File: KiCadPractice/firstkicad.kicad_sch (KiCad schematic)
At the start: 12 parts, among them Q1 BC337, U1 LM358, U2 LM358

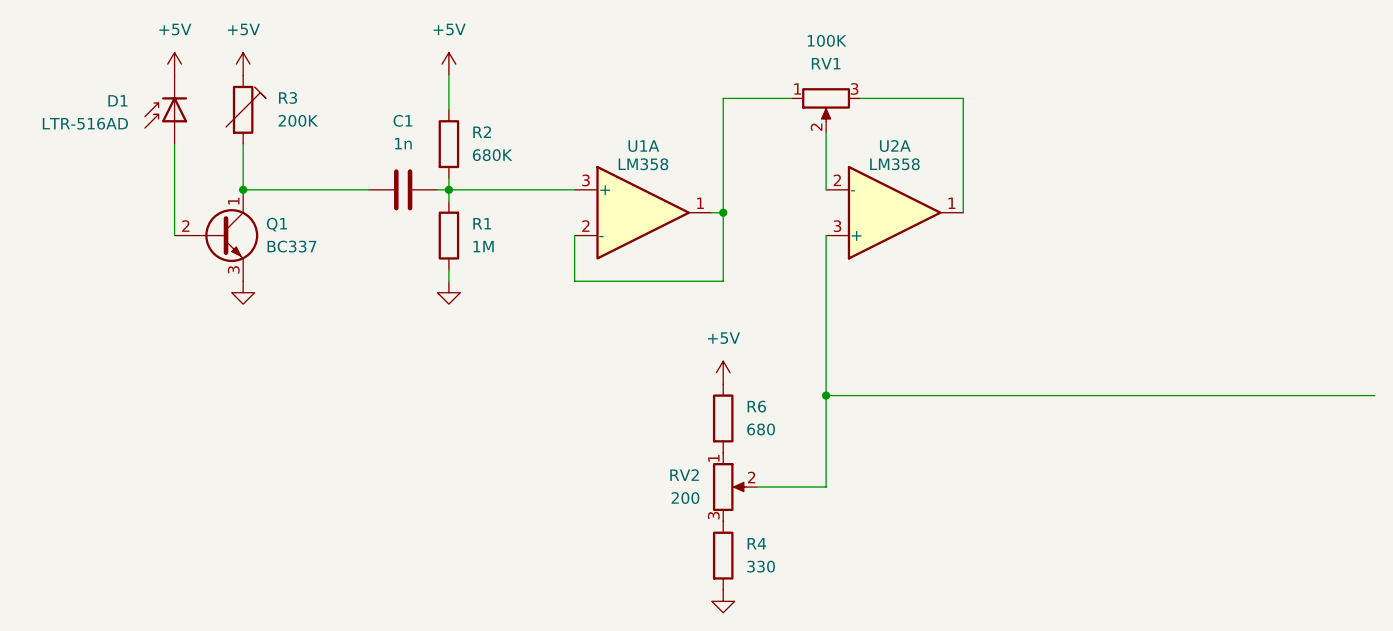
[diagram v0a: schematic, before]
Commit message: Fixed ERC issues.
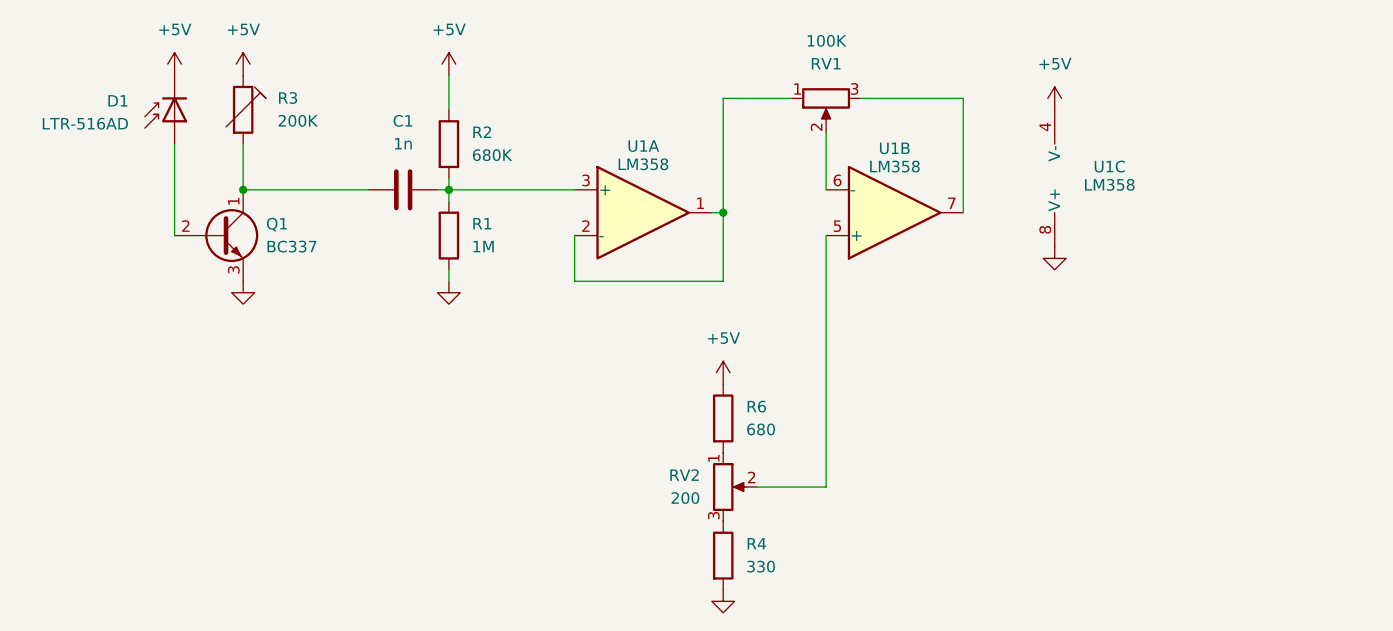
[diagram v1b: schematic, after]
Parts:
- added unit 3 of U1
- renumbered U2 to U1
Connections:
- net +5V: now also U1.4 (V-)
- net GND: now also U1.8 (V+)
- net at RV1.2: now also U1.6 (-); no longer U1.2 (-)
- net at RV1.3: now also U1.7; no longer U1.1
- net at RV2.2: now also U1.5 (+); no longer U1.3 (+)
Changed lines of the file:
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@@
 		(color 0 0 0 0)
 	)
-	(junction
-		(at 148.59 77.47)
-		(diameter 0)
-		(color 0 0 0 0)
-	)
 	(wire
 		(pts
@@
 	(wire
 		(pts
-			(xy 148.59 87.63) (xy 148.59 77.47)
+			(xy 148.59 59.69) (xy 148.59 87.63)
 		)
 		(stroke
@@
 	(wire
 		(pts
-			(xy 148.59 77.47) (xy 209.55 77.47)
-		)
-		(stroke
-			(width 0)
-			(type default)
-		)
-	)
-	(wire
-		(pts
 			(xy 106.68 54.61) (xy 120.65 54.61)
 		)
@@
 		(pts
 			(xy 83.82 54.61) (xy 97.79 54.61)
-		)
-		(stroke
-			(width 0)
-			(type default)
-		)
-	)
-	(wire
-		(pts
-			(xy 148.59 77.47) (xy 148.59 59.69)
 		)
 		(stroke
@@
 	(symbol
 		(lib_id "power:GND")
+		(at 173.99 60.96 0)
+		(unit 1)
+		(exclude_from_sim no)
+		(in_bom yes)
+		(on_board yes)
+		(dnp no)
+		(fields_autoplaced yes)
+		(property "Reference" "#PWR09"
+			(at 173.99 67.31 0)
+			(effects
+				(font
+					(size 1.27 1.27)
+				)
+				(hide yes)
+			)
+		)
+		(property "Value" "GND"
+			(at 173.99 66.04 0)
+			(effects
+				(font
+					(size 1.27 1.27)
+				)
+				(hide yes)
+			)
+		)
+		(property "Footprint" ""
+			(at 173.99 60.96 0)
+			(effects
+				(font
+					(size 1.27 1.27)
+				)
+				(hide yes)
+			)
+		)
+		(property "Datasheet" ""
+			(at 173.99 60.96 0)
+			(effects
+				(font
+					(size 1.27 1.27)
+				)
+				(hide yes)
+			)
+		)
+		(property "Description" "Power symbol creates a global label with name \"GND\" , ground"
+			(at 173.99 60.96 0)
+			(effects
+				(font
+					(size 1.27 1.27)
+				)
+				(hide yes)
+			)
+		)
+		(pin "1"
+		)
+		(instances
+			(project "firstkicad"
+				(path "/6a1506e1-f232-4ea9-a704-c10ff0d0d683"
+					(reference "#PWR09")
+					(unit 1)
+				)
+			)
+		)
+	)
+	(symbol
+		(lib_id "power:GND")
 		(at 137.16 99.06 0)
 		(unit 1)
@@
 	)
 	(symbol
+		(lib_id "Amplifier_Operational:LM358")
+		(at 176.53 53.34 0)
+		(mirror x)
+		(unit 3)
+		(exclude_from_sim no)
+		(in_bom yes)
+		(on_board yes)
+		(dnp no)
+		(property "Reference" "U1"
+			(at 180.086 52.07 0)
+			(effects
+				(font
+					(size 1.27 1.27)
+				)
+			)
+		)
+		(property "Value" "LM358"
+			(at 180.086 54.102 0)
+			(effects
+				(font
+					(size 1.27 1.27)
+				)
+			)
+		)
+		(property "Footprint" "OptoDevice:Broadcom_APDS-9160-003"
+			(at 176.53 53.34 0)
+			(effects
+				(font
+					(size 1.27 1.27)
+				)
+				(hide yes)
+			)
+		)
+		(property "Datasheet" "http://www.ti.com/lit/ds/symlink/lm2904-n.pdf"
+			(at 176.53 53.34 0)
+			(effects
+				(font
+					(size 1.27 1.27)
+				)
+				(hide yes)
+			)
+		)
+		(property "Description" "Low-Power, Dual Operational Amplifiers, DIP-8/SOIC-8/TO-99-8"
+			(at 176.53 53.34 0)
+			(effects
+				(font
+					(size 1.27 1.27)
+				)
+				(hide yes)
+			)
+		)
+		(pin "8"
+		)
+		(pin "5"
+		)
+		(pin "6"
+		)
+		(pin "7"
+		)
+		(pin "2"
+		)
+		(pin "3"
+		)
+		(pin "1"
+		)
+		(pin "4"
+		)
+		(instances
+			(project "firstkicad"
+				(path "/6a1506e1-f232-4ea9-a704-c10ff0d0d683"
+					(reference "U1")
+					(unit 3)
+				)
+			)
+		)
+	)
+	(symbol
 		(lib_id "power:+5V")
 		(at 83.82 41.91 0)
@@
 		(at 156.21 57.15 0)
 		(mirror x)
-		(unit 1)
-		(exclude_from_sim no)
-		(in_bom yes)
-		(on_board yes)
-		(dnp no)
-		(property "Reference" "U2"
-			(at 156.21 49.784 0)
+		(unit 2)
+		(exclude_from_sim no)
+		(in_bom yes)
+		(on_board yes)
+		(dnp no)
+		(property "Reference" "U1"
+			(at 156.21 50.038 0)
 			(effects
 				(font
@@
 		)
 		(property "Value" "LM358"
-			(at 156.21 51.816 0)
+			(at 156.21 52.07 0)
 			(effects
 				(font
@@
 			(project ""
 				(path "/6a1506e1-f232-4ea9-a704-c10ff0d0d683"
-					(reference "U2")
-					(unit 1)
-				)
+					(reference "U1")
+					(unit 2)
+				)
+			)
+		)
+	)
+	(symbol
+		(lib_id "power:+5V")
+		(at 173.99 45.72 0)
+		(unit 1)
+		(exclude_from_sim no)
+		(in_bom yes)
+		(on_board yes)
+		(dnp no)
+		(fields_autoplaced yes)
+		(property "Reference" "#PWR07"
+			(at 173.99 49.53 0)
+			(effects
+				(font
+					(size 1.27 1.27)
+				)
+				(hide yes)
+			)
+		)
+		(property "Value" "+5V"
+			(at 173.99 40.64 0)
+			(effects
+				(font
+					(size 1.27 1.27)
+				)
+			)
+		)
+		(property "Footprint" ""
+			(at 173.99 45.72 0)
+			(effects
+				(font
+					(size 1.27 1.27)
+				)
+				(hide yes)
+			)
+		)
+		(property "Datasheet" ""
+			(at 173.99 45.72 0)
+			(effects
+				(font
+					(size 1.27 1.27)
+				)
+				(hide yes)
+			)
+		)
+		(property "Description" "Power symbol creates a global label with name \"+5V\""
+			(at 173.99 45.72 0)
+			(effects
+				(font
+					(size 1.27 1.27)
+				)
+				(hide yes)
+			)
+		)
+		(pin "1"
+		)
+		(instances
+			(project "firstkicad"
+				(path "/6a1506e1-f232-4ea9-a704-c10ff0d0d683"
+					(reference "#PWR07")
+					(unit 1)
+				)

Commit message: Fixed footprints.
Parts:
- C1: footprint Capacitor_THT:CP_Axial_L30.0mm_D18.0mm_P35.00mm_Horizontal -> Capacitor_SMD:C_1206_3216Metric_Pad1.33x1.80mm_HandSolder
- D1: footprint Diode_THT:D_A-405_P5.08mm_Vertical_KathodeUp -> Library:LTR-516AD
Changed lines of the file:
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@@
 			)
 		)
-		(property "Footprint" "Diode_THT:D_A-405_P5.08mm_Vertical_KathodeUp"
+		(property "Footprint" "Library:LTR-516AD"
 			(at 76.2 45.72 0)
 			(effects
@@
 			)
 		)
-		(property "Footprint" "Capacitor_THT:CP_Axial_L30.0mm_D18.0mm_P35.00mm_Horizontal"
+		(property "Footprint" "Capacitor_SMD:C_1206_3216Metric_Pad1.33x1.80mm_HandSolder"
 			(at 105.41 53.6448 0)
 			(effects

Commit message: Patched some more footprints.
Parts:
- Q1: footprint Transformer_THT:Autotransformer_Toroid_1Tap_Horizontal_D10.5mm_Amidon-T37 -> Package_TO_SOT_THT:TO-92L_Inline
- R1, R2, R3, R4, R6: footprint Resistor_THT:R_Axial_DIN0204_L3.6mm_D1.6mm_P7.62mm_Horizontal -> Resistor_SMD:R_1206_3216Metric_Pad1.30x1.75mm_HandSolder
- RV1, RV2: footprint Potentiometer_THT:Potentiometer_ACP_CA9-V10_Vertical_Hole -> Potentiometer_THT:Potentiometer_Bourns_3266W_Vertical
- U1: footprint OptoDevice:Broadcom_APDS-9160-003 -> Package_TO_SOT_SMD:SOT-23-8_Handsoldering
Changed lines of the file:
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@@
 			)
 		)
-		(property "Footprint" "Resistor_THT:R_Axial_DIN0204_L3.6mm_D1.6mm_P7.62mm_Horizontal"
+		(property "Footprint" "Resistor_SMD:R_1206_3216Metric_Pad1.30x1.75mm_HandSolder"
 			(at 135.382 95.25 90)
 			(effects
@@
 			)
 		)
-		(property "Footprint" "Resistor_THT:R_Axial_DIN0204_L3.6mm_D1.6mm_P7.62mm_Horizontal"
+		(property "Footprint" "Resistor_SMD:R_1206_3216Metric_Pad1.30x1.75mm_HandSolder"
 			(at 108.458 59.69 90)
 			(effects
@@
 			)
 		)
-		(property "Footprint" "Resistor_THT:R_Axial_DIN0204_L3.6mm_D1.6mm_P7.62mm_Horizontal"
+		(property "Footprint" "Resistor_SMD:R_1206_3216Metric_Pad1.30x1.75mm_HandSolder"
 			(at 104.902 49.53 90)
 			(effects
@@
 			)
 		)
-		(property "Footprint" "Potentiometer_THT:Potentiometer_ACP_CA9-V10_Vertical_Hole"
+		(property "Footprint" "Potentiometer_THT:Potentiometer_Bourns_3266W_Vertical"
 			(at 148.59 44.45 0)
 			(effects
@@
 			)
 		)
-		(property "Footprint" "OptoDevice:Broadcom_APDS-9160-003"
+		(property "Footprint" "Package_TO_SOT_SMD:SOT-23-8_Handsoldering"
 			(at 128.27 57.15 0)
 			(effects
@@
 			)
 		)
-		(property "Footprint" "Resistor_THT:R_Axial_DIN0204_L3.6mm_D1.6mm_P7.62mm_Horizontal"
+		(property "Footprint" "Resistor_SMD:R_1206_3216Metric_Pad1.30x1.75mm_HandSolder"
 			(at 135.382 80.01 90)
 			(effects
@@
 			)
 		)
-		(property "Footprint" "OptoDevice:Broadcom_APDS-9160-003"
+		(property "Footprint" "Package_TO_SOT_SMD:SOT-23-8_Handsoldering"
 			(at 176.53 53.34 0)
 			(effects
@@
 			)
 		)
-		(property "Footprint" "Resistor_THT:R_Axial_DIN0204_L3.6mm_D1.6mm_P7.62mm_Horizontal"
+		(property "Footprint" "Resistor_SMD:R_1206_3216Metric_Pad1.30x1.75mm_HandSolder"
 			(at 82.042 45.72 90)
 			(effects
@@
 			)
 		)
-		(property "Footprint" "Transformer_THT:Autotransformer_Toroid_1Tap_Horizontal_D10.5mm_Amidon-T37"
+		(property "Footprint" "Package_TO_SOT_THT:TO-92L_Inline"
 			(at 86.36 61.595 0)
 			(effects
@@
 			)
 		)
-		(property "Footprint" "OptoDevice:Broadcom_APDS-9160-003"
+		(property "Footprint" "Package_TO_SOT_SMD:SOT-23-8_Handsoldering"
 			(at 156.21 57.15 0)
 			(effects
@@
 			)
 		)
-		(property "Footprint" "Potentiometer_THT:Potentiometer_ACP_CA9-V10_Vertical_Hole"
+		(property "Footprint" "Potentiometer_THT:Potentiometer_Bourns_3266W_Vertical"
 			(at 137.16 87.63 0)
 			(effects
